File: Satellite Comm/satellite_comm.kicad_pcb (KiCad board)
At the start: 2 copper layers, 139.7 x 100.3 mm, 10 parts, among them J1 RockBlock Connector, J2 PC104_40Pin_2.54mm-WhitworthS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, U1 SAM-M8Q

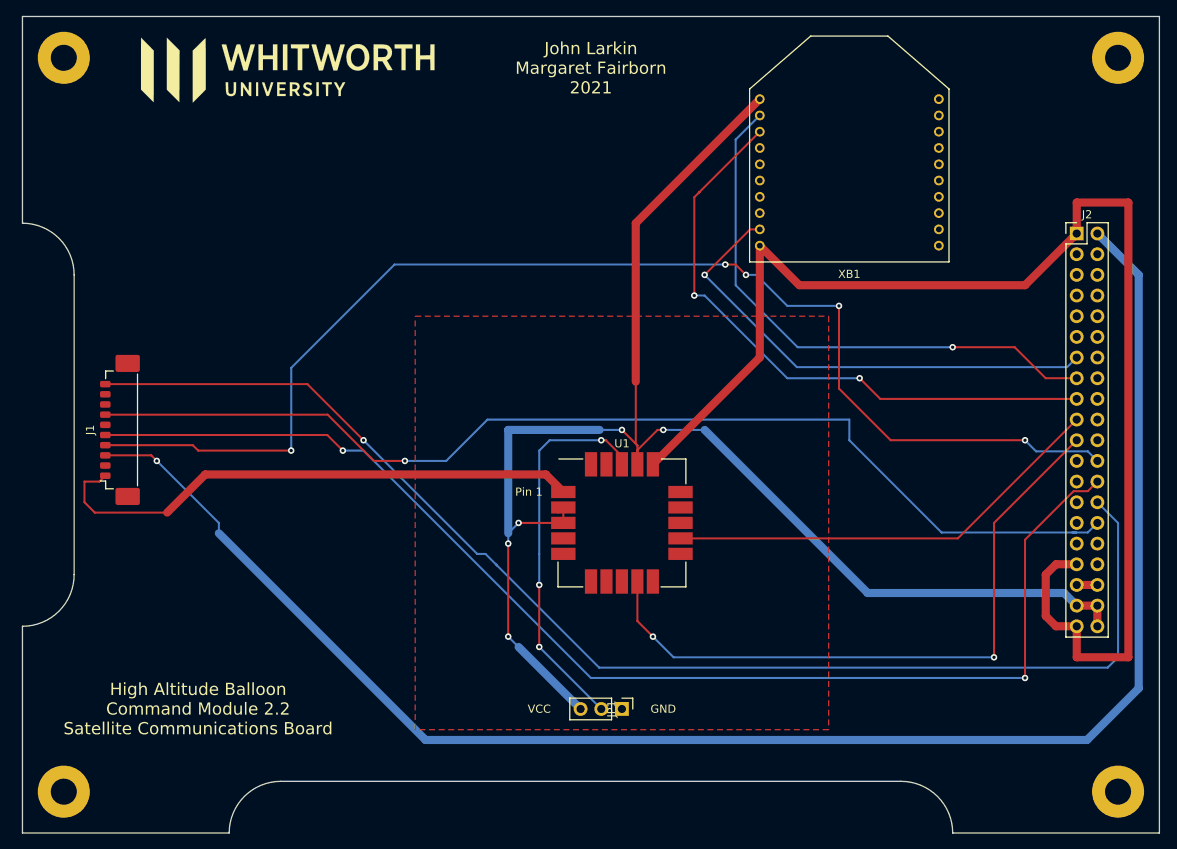
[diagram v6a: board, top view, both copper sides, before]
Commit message: made the weird small trails thicker
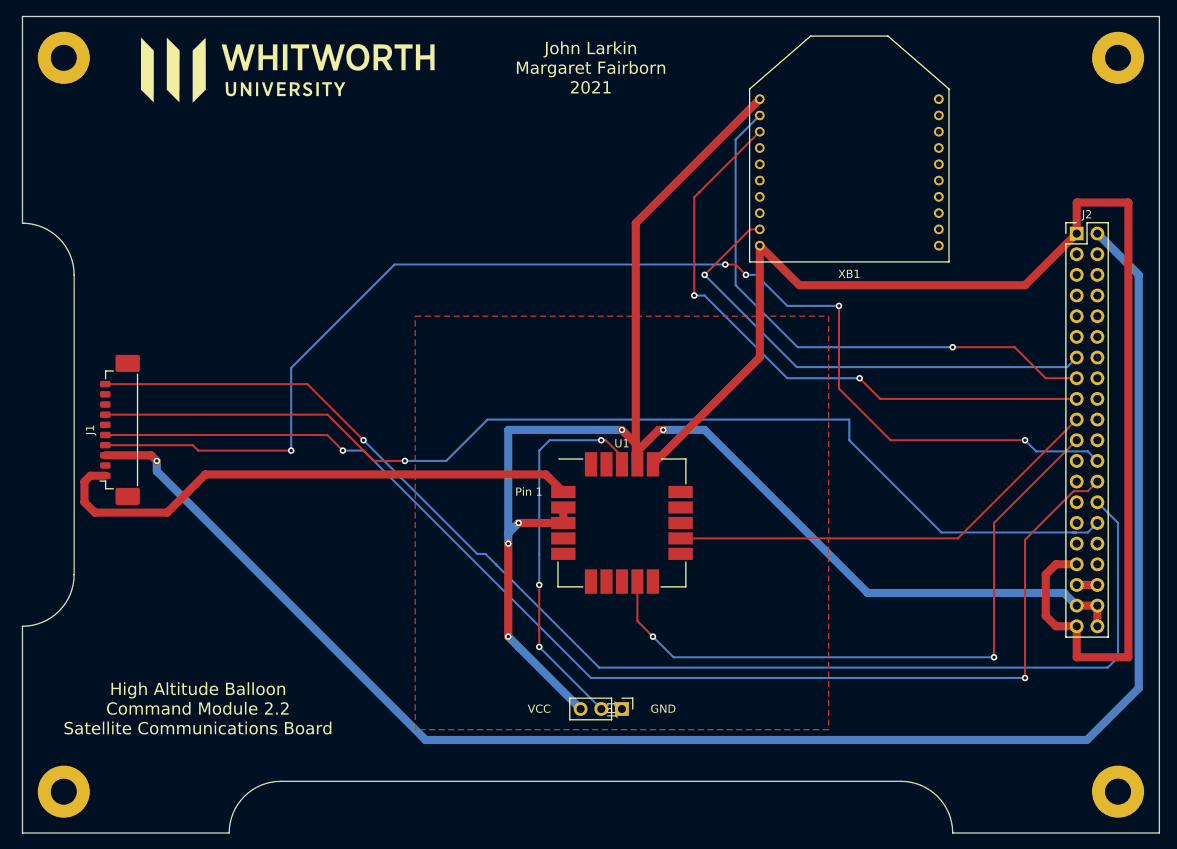
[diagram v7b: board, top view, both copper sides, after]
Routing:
- net +3V3: track 187.8 -> 191.8 mm
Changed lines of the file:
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@@
     (thickness 1.6)
     (drawings 25)
-    (tracks 175)
+    (tracks 176)
     (zones 0)
     (modules 10)
@@
   (segment (start 116 67.29) (end 102.86 80.43) (width 1) (layer F.Cu) (net 1))
   (segment (start 116 53.56) (end 116 67.29) (width 1) (layer F.Cu) (net 1))
-  (segment (start 89.70501 81.67501) (end 47.86499 81.67501) (width 1) (layer F.Cu) (net 1))
-  (segment (start 91.86 83.83) (end 89.70501 81.67501) (width 1) (layer F.Cu) (net 1))
-  (segment (start 47.86499 81.67501) (end 43.18 86.36) (width 1) (layer F.Cu) (net 1))
-  (segment (start 43.18 86.36) (end 34.29 86.36) (width 0.25) (layer F.Cu) (net 1))
   (segment (start 116 53.56) (end 120.86 58.42) (width 1) (layer F.Cu) (net 1))
   (segment (start 148.59 58.42) (end 154.94 52.07) (width 1) (layer F.Cu) (net 1))
   (segment (start 120.86 58.42) (end 148.59 58.42) (width 1) (layer F.Cu) (net 1))
-  (segment (start 34.855 82.55) (end 35.58 81.825) (width 0.25) (layer F.Cu) (net 1))
-  (segment (start 34.29 86.36) (end 33.02 85.09) (width 0.25) (layer F.Cu) (net 1))
-  (segment (start 33.02 82.55) (end 34.855 82.55) (width 0.25) (layer F.Cu) (net 1))
-  (segment (start 33.02 85.09) (end 33.02 82.55) (width 0.25) (layer F.Cu) (net 1))
   (segment (start 154.94 92.71) (end 152.4 92.71) (width 1) (layer F.Cu) (net 1))
   (segment (start 152.4 92.71) (end 151.13 93.98) (width 1) (layer F.Cu) (net 1))
@@
   (segment (start 161.29 104.14) (end 154.94 104.14) (width 1) (layer F.Cu) (net 1))
   (segment (start 154.94 104.14) (end 154.94 100.33) (width 1) (layer F.Cu) (net 1))
+  (segment (start 47.86499 81.67501) (end 89.70501 81.67501) (width 1) (layer F.Cu) (net 1))
+  (segment (start 43.18 86.36) (end 47.86499 81.67501) (width 1) (layer F.Cu) (net 1))
+  (segment (start 33.02 85.09) (end 34.29 86.36) (width 1) (layer F.Cu) (net 1))
+  (segment (start 34.29 86.36) (end 43.18 86.36) (width 1) (layer F.Cu) (net 1))
+  (segment (start 89.70501 81.67501) (end 91.86 83.83) (width 1) (layer F.Cu) (net 1))
+  (segment (start 35.58 81.825) (end 33.745 81.825) (width 1) (layer F.Cu) (net 1))
+  (segment (start 33.02 82.55) (end 33.02 85.09) (width 1) (layer F.Cu) (net 1))
+  (segment (start 33.745 81.825) (end 33.02 82.55) (width 1) (layer F.Cu) (net 1))
   (via (at 41.91 80.01) (size 0.8) (drill 0.4) (layers F.Cu B.Cu) (net 2))
-  (segment (start 49.53 87.63) (end 41.91 80.01) (width 0.25) (layer B.Cu) (net 2))
-  (segment (start 49.53 88.9) (end 49.53 87.63) (width 0.25) (layer B.Cu) (net 2))
-  (segment (start 41.225 79.325) (end 35.58 79.325) (width 0.25) (layer F.Cu) (net 2))
-  (segment (start 41.91 80.01) (end 41.225 79.325) (width 0.25) (layer F.Cu) (net 2))
-  (segment (start 156.21 114.3) (end 74.93 114.3) (width 1) (layer B.Cu) (net 2))
-  (segment (start 162.56 107.95) (end 156.21 114.3) (width 1) (layer B.Cu) (net 2))
-  (segment (start 162.56 57.15) (end 162.56 107.95) (width 1) (layer B.Cu) (net 2))
-  (segment (start 74.93 114.3) (end 49.53 88.9) (width 1) (layer B.Cu) (net 2))
-  (segment (start 157.48 52.07) (end 162.56 57.15) (width 1) (layer B.Cu) (net 2))
+  (segment (start 162.56 57.15) (end 157.48 52.07) (width 1) (layer B.Cu) (net 2))
+  (segment (start 156.21 114.3) (end 162.56 107.95) (width 1) (layer B.Cu) (net 2))
+  (segment (start 74.93 114.3) (end 156.21 114.3) (width 1) (layer B.Cu) (net 2))
+  (segment (start 41.91 81.28) (end 74.93 114.3) (width 1) (layer B.Cu) (net 2))
+  (segment (start 162.56 107.95) (end 162.56 57.15) (width 1) (layer B.Cu) (net 2))
+  (segment (start 41.91 80.01) (end 41.91 81.28) (width 1) (layer B.Cu) (net 2))
+  (segment (start 41.225 79.325) (end 41.91 80.01) (width 1) (layer F.Cu) (net 2))
+  (segment (start 35.58 79.325) (end 41.225 79.325) (width 1) (layer F.Cu) (net 2))
   (segment (start 100.96 99.69) (end 102.87 101.6) (width 0.25) (layer F.Cu) (net 6))
   (via (at 102.87 101.6) (size 0.8) (drill 0.4) (layers F.Cu B.Cu) (net 6))
@@
   (segment (start 148.59 77.47) (end 149.954999 78.834999) (width 0.25) (layer B.Cu) (net 22))
   (segment (start 91.23 86.36) (end 91.86 85.73) (width 0.25) (layer F.Cu) (net 23))
-  (segment (start 100.96 78.68) (end 100.96 80.43) (width 0.25) (layer F.Cu) (net 23))
-  (segment (start 103.44 76.2) (end 100.96 78.68) (width 0.25) (layer F.Cu) (net 23))
   (via (at 104.14 76.2) (size 0.8) (drill 0.4) (layers F.Cu B.Cu) (net 23))
-  (segment (start 103.44 76.2) (end 104.14 76.2) (width 0.25) (layer F.Cu) (net 23))
   (segment (start 100.96 79.37) (end 100.96 80.43) (width 0.25) (layer F.Cu) (net 23))
   (via (at 86.36 87.63) (size 0.8) (drill 0.4) (layers F.Cu B.Cu) (net 23))
-  (segment (start 86.36 87.63) (end 91.86 87.63) (width 0.25) (layer F.Cu) (net 23))
-  (segment (start 91.86 87.63) (end 91.86 85.73) (width 0.25) (layer F.Cu) (net 23))
   (segment (start 85.09 90.17) (end 85.09 90.17) (width 0.25) (layer B.Cu) (net 23))
   (via (at 99.06 76.2) (size 0.8) (drill 0.4) (layers F.Cu B.Cu) (net 23))
-  (segment (start 96.323002 76.2) (end 99.06 76.2) (width 0.25) (layer B.Cu) (net 23))
-  (segment (start 99.06 76.2) (end 100.96 78.1) (width 0.25) (layer F.Cu) (net 23))
-  (segment (start 85.09 88.9) (end 86.36 87.63) (width 0.25) (layer B.Cu) (net 23))
-  (segment (start 109.22 76.2) (end 104.14 76.2) (width 0.25) (layer B.Cu) (net 23))
-  (segment (start 116 35.56) (end 100.76 50.8) (width 1) (layer F.Cu) (net 23))
-  (segment (start 100.76 50.8) (end 100.76 70.28) (width 1) (layer F.Cu) (net 23))
   (segment (start 100.76 77.91) (end 100.96 78.11) (width 0.25) (layer F.Cu) (net 23))
   (segment (start 100.96 78.11) (end 100.96 80.43) (width 0.25) (layer F.Cu) (net 23))
-  (segment (start 100.76 70.28) (end 100.76 77.91) (width 0.25) (layer F.Cu) (net 23))
   (segment (start 100.96 78.1) (end 100.96 78.11) (width 0.25) (layer F.Cu) (net 23))
-  (segment (start 85.09 90.17) (end 85.09 88.9) (width 0.25) (layer B.Cu) (net 23))
   (via (at 85.09 90.17) (size 0.8) (drill 0.4) (layers F.Cu B.Cu) (net 23))
-  (segment (start 85.09 90.17) (end 85.09 101.6) (width 0.25) (layer F.Cu) (net 23))
   (segment (start 154.94 97.79) (end 157.48 97.79) (width 1) (layer F.Cu) (net 23))
   (segment (start 157.48 97.79) (end 157.48 100.33) (width 1) (layer F.Cu) (net 23))
@@
   (segment (start 85.09 76.2) (end 96.323002 76.2) (width 1) (layer B.Cu) (net 23))
   (segment (start 93.98 110.49) (end 86.36 102.87) (width 1) (layer B.Cu) (net 23))
-  (segment (start 86.36 102.87) (end 85.09 101.6) (width 0.25) (layer B.Cu) (net 23))
+  (segment (start 109.22 76.2) (end 104.14 76.2) (width 1) (layer B.Cu) (net 23))
+  (segment (start 100.96 78.68) (end 100.96 80.43) (width 0.25) (layer F.Cu) (net 23))
+  (segment (start 100.96 78.814315) (end 100.96 80.43) (width 1) (layer F.Cu) (net 23))
+  (segment (start 103.574315 76.2) (end 100.96 78.814315) (width 1) (layer F.Cu) (net 23))
+  (segment (start 104.14 76.2) (end 103.574315 76.2) (width 1) (layer F.Cu) (net 23))
+  (segment (start 100.76 80.23) (end 100.96 80.43) (width 1) (layer F.Cu) (net 23))
+  (segment (start 116 35.56) (end 100.76 50.8) (width 1) (layer F.Cu) (net 23))
+  (segment (start 99.06 76.2) (end 100.76 77.9) (width 1) (layer F.Cu) (net 23))
+  (segment (start 100.76 77.9) (end 100.76 80.23) (width 1) (layer F.Cu) (net 23))
+  (segment (start 100.76 50.8) (end 100.76 77.9) (width 1) (layer F.Cu) (net 23))
+  (segment (start 96.323002 76.2) (end 99.06 76.2) (width 1) (layer B.Cu) (net 23))
+  (segment (start 85.09 88.9) (end 86.36 87.63) (width 1) (layer B.Cu) (net 23))
+  (segment (start 86.36 87.63) (end 91.86 87.63) (width 1) (layer F.Cu) (net 23))
+  (segment (start 91.86 85.73) (end 91.86 87.63) (width 1) (layer F.Cu) (net 23))
+  (segment (start 85.09 88.9) (end 85.09 90.17) (width 1) (layer B.Cu) (net 23))
+  (segment (start 85.09 90.17) (end 85.09 101.6) (width 1) (layer F.Cu) (net 23))
+  (segment (start 85.09 101.6) (end 86.36 102.87) (width 1) (layer B.Cu) (net 23))
   (segment (start 154.94 95.25) (end 157.48 95.25) (width 1) (layer F.Cu) (net 24))
   (via (at 96.52 77.47) (size 0.8) (drill 0.4) (layers F.Cu B.Cu) (net 32))

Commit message: Made unimportant aesthetic changes...
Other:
- board text added: "Meg Fairborn John Larkin 2021"
- board text removed: "John Larkin Margaret Fairborn 2021"
